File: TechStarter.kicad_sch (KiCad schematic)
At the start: 35 parts, among them J1 Conn_01x04_Socket, J10 Conn_01x03_Socket, J11 Conn_01x03_Socket, J12 Conn_01x04_Pin, J2 Conn_01x04_Socket, J3 Conn_01x02_Socket, J4 Conn_01x04_Socket, J5 Conn_01x03_Socket, J6 Conn_01x04_Socket, J7 Conn_01x03_Socket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

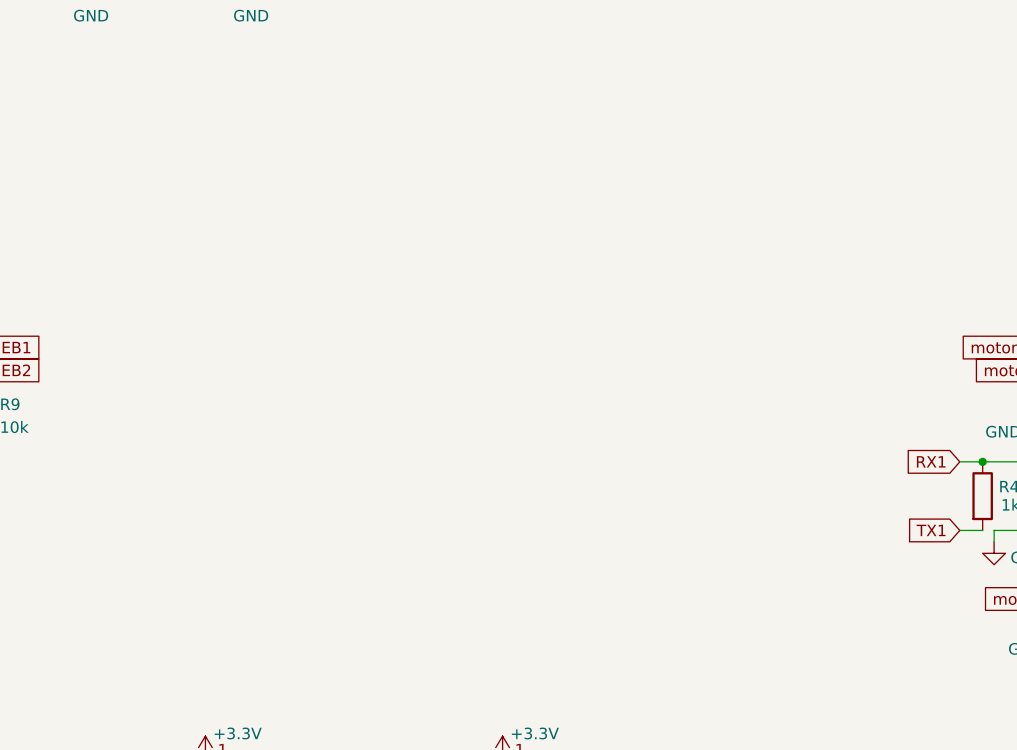
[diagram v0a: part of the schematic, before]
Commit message: Robot I/O
připojil jsem výstup a input z robota přes optočleny a přidal konektor na napájení 24 V
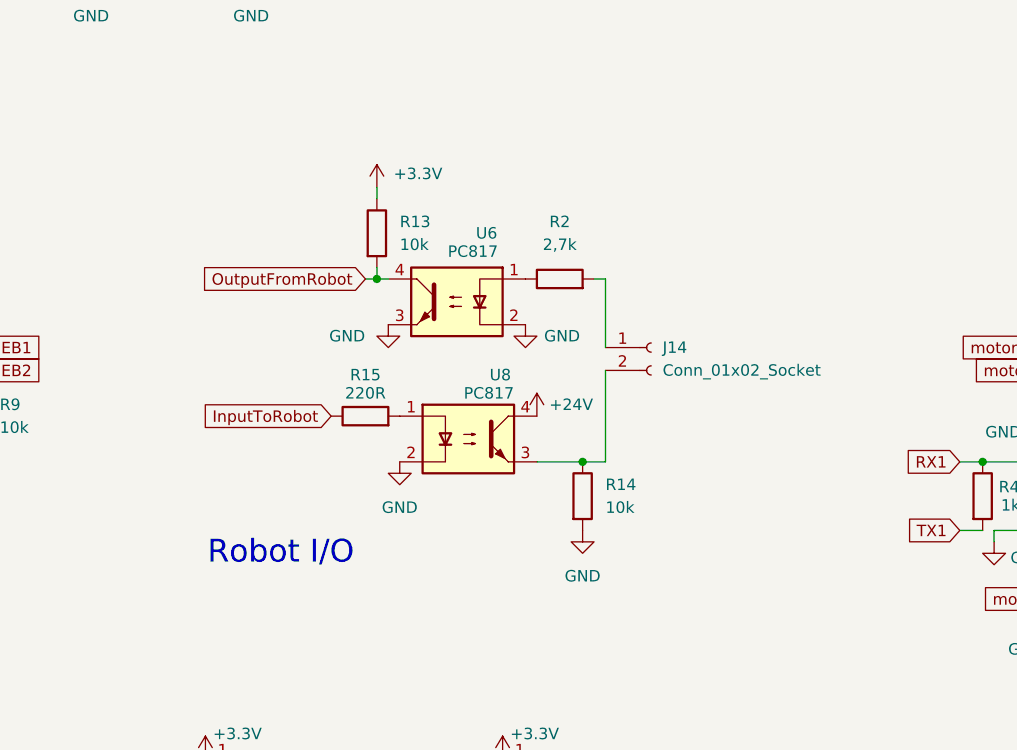
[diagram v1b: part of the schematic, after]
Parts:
- added J14: Conn_01x02_Socket, Connector:JWT_A3963_1x02_P3.96mm_Vertical, symbol Connector:Conn_01x02_Socket
- added R13, R14: 10k, symbol Device:R
- added R15: 220R, symbol Device:R
- added R2: 2,7k, symbol Device:R
- added U6, U8: PC817, Package_DIP:DIP-4_W7.62mm, symbol Isolator:PC817
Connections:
- net +24V: now also U8.4
- net +3.3V: now also R13.1
- net GND: now also R14.2, U6.2, U6.3, U8.2
- new net: R2.1, U6.1
- new net: J14.2 (Pin_2), R14.1, U8.3
- new net: R15.2, U8.1
- new net: J14.1 (Pin_1), R2.2
- new net InputToRobot: R15.1
- new net OutputFromRobot: R13.2, U6.4
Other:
- note added: "Robot I/O"

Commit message: .
sortation of things, added variant B
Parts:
- removed D2: 1N5408, Diode_THT:D_DO-201AD_P15.24mm_Horizontal, symbol Diode:1N5408
- removed J14: Conn_01x02_Socket, Connector:JWT_A3963_1x02_P3.96mm_Vertical, symbol Connector:Conn_01x02_Socket
- removed J3: Conn_01x02_Socket, symbol Connector:Conn_01x02_Socket
- removed J4, J6: Conn_01x04_Socket, symbol Connector:Conn_01x04_Socket
- removed Q2: IRLZ44N, Package_TO_SOT_THT:TO-220-3_Vertical, symbol Transistor_FET:IRLZ44N
- removed R11, R13, R14: 10k, symbol Device:R
- removed R12: 100R, symbol Device:R
- removed R15: 220R, symbol Device:R
- removed R2: 2,7k, symbol Device:R
- removed U6, U8: PC817, Package_DIP:DIP-4_W7.62mm, symbol Isolator:PC817
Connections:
- net +BATT is gone; now on net +3.3V: BT1.1 (+), U1.1 (VBAT)
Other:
- added sheet OUTPUT BLOCK (Logic block.kicad_sch)
- note removed: "Display"
- note removed: "End buttons"
- note removed: "Inductor for pneumatic rotaty thing"
- note removed: "Robot I/O"
- moved on the sheet: BT1, J12, U5

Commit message: Board
started board ...
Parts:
- removed C1: 2,2u/6,3V, Connector_JST:JST_XH_S3B-XH-A_1x03_P2.50mm_Horizontal, symbol Device:C_Small
- removed C2, C4: 100n/16V, symbol Device:C_Small
- removed C3, C5: 22n/50V, symbol Device:C_Small
- removed C6: 2,2u/6,3V, symbol Device:C_Small
- removed J1, J2: Conn_01x04_Socket, symbol Connector:Conn_01x04_Socket
- removed R5, R6, R7, R8: 0,11R, symbol Device:R
- removed U2, U3: TMC2209-LA, Package_DFN_QFN:VQFN-28-1EP_5x5mm_P0.5mm_EP3.7x3.7mm_ThermalVias, symbol Driver_Motor:TMC2209-LA
- added R2: 1k, Resistor_SMD:R_0603_1608Metric, symbol Device:R
- R10, R9: footprint (none) -> Resistor_SMD:R_0603_1608Metric
- R3, R4: value 1k -> 10k; footprint (none) -> Resistor_SMD:R_0603_1608Metric
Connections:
- net EB1: now also R9.1; no longer R10.1
- net EB2: now also R10.1; no longer R9.1
- net GND: now also R3.2, R4.2
- net motor1dir: now also U1.20 (PA4); no longer U1.14 (PA0)
- net motor1step: now also U1.14 (PA0); no longer U1.15 (PA1)
- net motor2dir: now also U1.21 (PA5); no longer U1.17 (PA3)
- net motor2step: now also U1.15 (PA1); no longer U1.20 (PA4)
- net motorEN: now also U1.8 (PC0)
- net InputToRobot: now reaches U1.10 (PC2)
- net motor3step: now reaches U1.16 (PA2)
- net motor3dir: now reaches U1.22 (PA6)
- net motor4dir: now reaches U1.23 (PA7)
- net Inductor: now reaches U1.41 (PA8)
- net EB3: now reaches U1.61 (PB8)
- net EB3: now also R3.1
- net EB4: now reaches U1.62 (PB9)
- net EB4: now also R4.1
- net OutputFromRobot: now reaches U1.9 (PC1)
- removed net RX1: R3.1, R4.1, U1.43 (PA10)
- removed net TX1: R3.2, R4.2, U1.42 (PA9)
- new net RX1/TX1: R2.2, U1.43 (PA10)
- new net TX1/RX1: R2.1, U1.42 (PA9)
- new net motor4step: U1.17 (PA3)
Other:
- moved on the sheet: BT1, R10, R9, U1, U5

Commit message: .
.
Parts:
- removed BT1: Battery_Cell, Battery:BatteryHolder_ComfortableElectronic_CH273-2450_1x2450, symbol Device:Battery_Cell
- added C17: 680uF/35V, Capacitor_SMD:C_Elec_10x10.2, symbol Device:C
- added C21: 4,7uF, Capacitor_SMD:C_Elec_10x10.2, symbol Device:C
- added R5, R6: 10k, Resistor_SMD:R_0603_1608Metric, symbol Device:R
- J12: footprint (none) -> Connector_PinSocket_2.54mm:PinSocket_1x04_P2.54mm_Vertical_SMD_Pin1Left
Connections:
- net +3.3V: now also R6.1
- net GND: now also C17.2, C21.2, R5.2
- net Vbat: now reaches U1.11 (PC3)
- net at U1.30 (VCAP_1): now also C21.1
- net at U1.60 (BOOT0): now also R5.1
- net at U1.7 (NRST): now also C17.1, R6.2
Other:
- moved on the sheet: J12

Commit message: Capacitor + other stuff
Did a safe of your ass
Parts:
- C17: value 680uF/35V -> 100n/6,3V; footprint Capacitor_SMD:C_Elec_10x10.2 -> Capacitor_SMD:C_0603_1608Metric
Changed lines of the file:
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@@
 			)
 		)
-		(property "Value" "680uF/35V"
+		(property "Value" "100n/6,3V"
 			(at 29.464 45.72 0)
 			(effects
@@
 			)
 		)
-		(property "Footprint" "Capacitor_SMD:C_Elec_10x10.2"
+		(property "Footprint" "Capacitor_SMD:C_0603_1608Metric"
 			(at 44.1452 48.26 0)
 			(effects

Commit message: ,
,
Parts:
- added FID1, FID2, FID3, FID4, FID5, FID6, FID7, FID8: Fiducial, Fiducial:Fiducial_0.75mm_Mask1.5mm, symbol Mechanical:Fiducial
